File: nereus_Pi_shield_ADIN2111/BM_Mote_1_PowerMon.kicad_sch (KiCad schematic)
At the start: 4 parts, among them U4 INA232AIDDFR

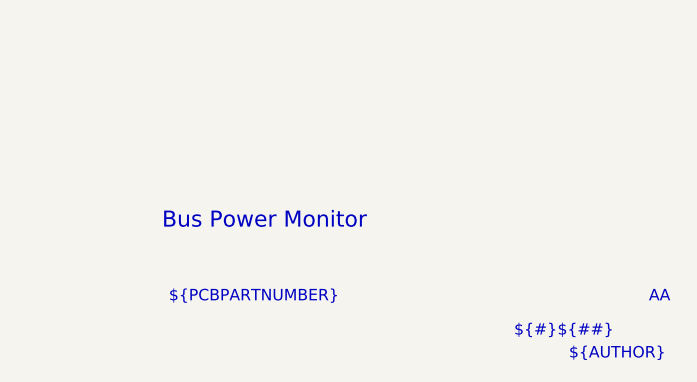
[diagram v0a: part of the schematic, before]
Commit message: S6.g: presentation clean-up (Nick's list) + active-low names (D30)
- Top-Level: VBUS_OUT beside the Load Switch; I2C page-long runs ->
  labelled stubs at the PoDL pins; R43 beside the ADIN HW_EN pin; J5
  spaced with its note
- Cover: mote renders + old index -> grey TBD box + real sheet index;
  dimensions TBD; revision table inside the page, about this board;
  licence note and CC logo clear of the title block
- ADIN: supplies and LED blocks spaced from U1A, with headers
- Power: 3V3 / 1V8 / 5V converters spaced, with headers
- All sheets: KiCad title block filled; Altium overlay texts removed
- Names: ~{ADIN_RST}, ~{ADIN_INT}, ~{ADIN_CS}, ~{ADIN_P1/P2_LED1},
  PAYLOAD_EN, ~{PAYLOAD_FAULT} (labels, hier labels, sheet pins)
- Same pin partition; ERC 495 -> 492 / 0 errors; 8 exclusion keys
  regenerated (reasons unchanged); netcheck 51/51; midwire 0
- Docs: DESIGN D30 + pin map, changelog, README, sofar_brief, TRACKER,
  viewer, DEV_LOG; schematic.pdf re-exported

Co-Authored-By: Claude Opus 5.5 <noreply@anthropic.com>
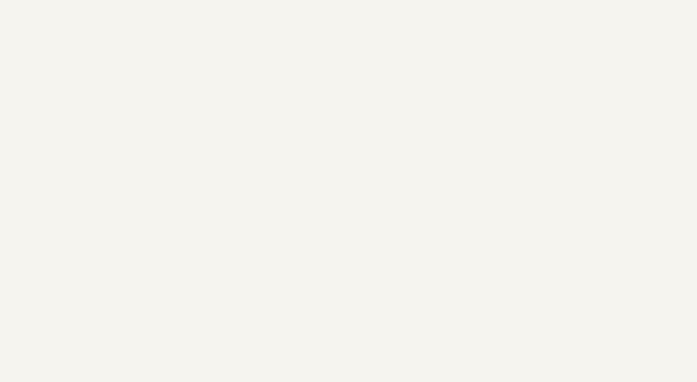
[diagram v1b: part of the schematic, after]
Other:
- note removed: "${##}"
- note removed: "${#}"
- note removed: "${AUTHOR}"
- note removed: "${PCBPARTNUMBER}"
- note removed: "${REVISION}"
- note removed: "${TITLE}"
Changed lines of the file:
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@@
 	(title_block
 		(title "Bus Power Monitor")
+		(date "2026-10-07")
 		(rev "AA")
-	)
-	(text "${#}"
-		(exclude_from_sim no)
-		(at 395.224 289.3822 0)
-		(effects
-			(font
-				(size 1.27 1.27)
-			)
-			(justify left bottom)
-		)
-	)
-	(text "${TITLE}"
-		(exclude_from_sim no)
-		(at 356.108 277.4442 0)
-		(effects
-			(font
-				(size 1.778 1.778)
-			)
-			(justify left bottom)
-		)
-	)
-	(text "${##}"
-		(exclude_from_sim no)
-		(at 400.05 289.3822 0)
-		(effects
-			(font
-				(size 1.27 1.27)
-			)
-			(justify left bottom)
-		)
-	)
-	(text "${PCBPARTNUMBER}"
-		(exclude_from_sim no)
-		(at 356.87 285.5722 0)
-		(effects
-			(font
-				(size 1.27 1.27)
-			)
-			(justify left bottom)
-		)
+		(comment 1 "${PCBPARTNAME} · ${PCBPARTNUMBER}")
+		(comment 2 "Author: ${AUTHOR}")
+		(comment 3 "Derived from Sofar Bristlemouth mote 000639-AB")
 	)
 	(text "I2C Address: 0x41"
@@
 			)
 			(justify left bottom)
-		)
-	)
-	(text "${REVISION}"
-		(exclude_from_sim no)
-		(at 410.21 285.5722 0)
-		(effects
-			(font
-				(size 1.27 1.27)
-			)
-			(justify left bottom)
-		)
-	)
-	(text "${AUTHOR}"
-		(exclude_from_sim no)
-		(at 401.32 291.9222 0)
-		(effects
-			(font
-				(size 1.27 1.27)
-			)
-			(justify left bottom)
